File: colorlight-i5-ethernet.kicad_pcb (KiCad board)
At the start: 2 copper layers, 44 x 43.5 mm, 6 parts, among them J1 P1, J2 48F-01GY2DPL2NL, J3 48F-01GY2DPL2NL

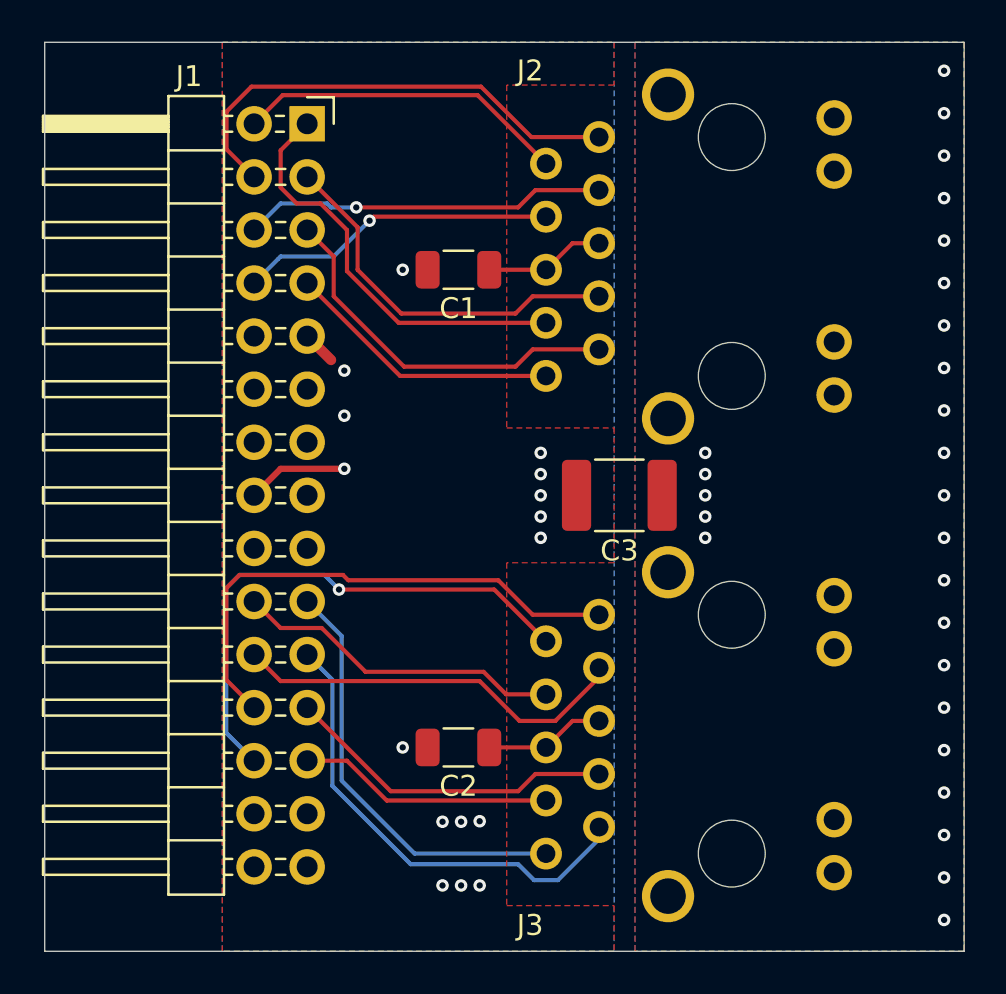
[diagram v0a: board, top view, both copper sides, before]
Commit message: Update to KiCad 6.0, prepare for production
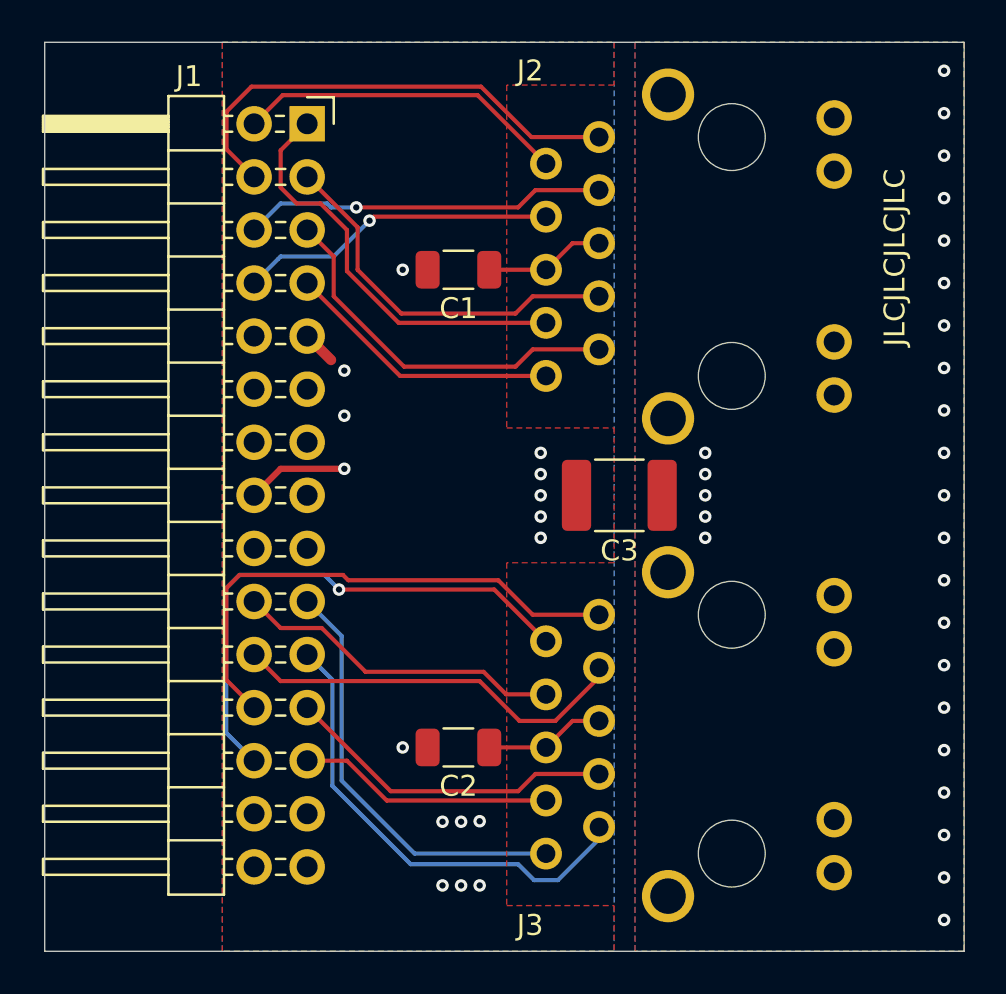
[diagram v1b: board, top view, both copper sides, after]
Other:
- net class Default removed
- net class Grounds removed
- board text added: "JLCJLCJLCJLC"
